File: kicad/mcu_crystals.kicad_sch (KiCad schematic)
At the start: 4 parts, among them X1 32MHz, X2 32kHz768

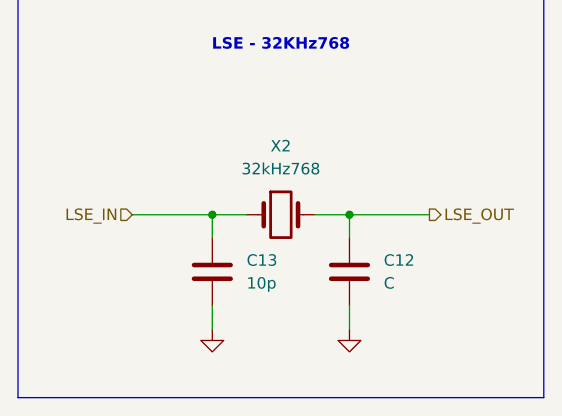
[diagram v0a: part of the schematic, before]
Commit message: fix(schematic:crystals): add the missing value for C12; 10pF
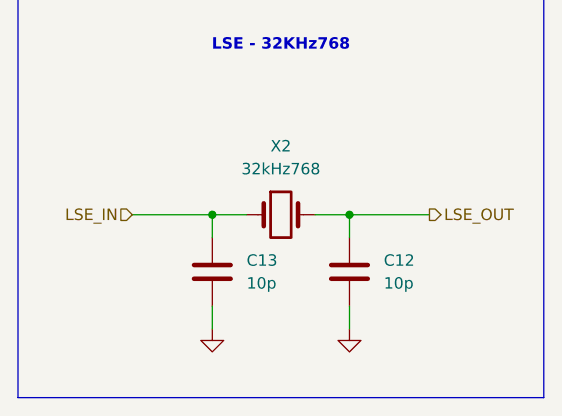
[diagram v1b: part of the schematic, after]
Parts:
- C12: value C -> 10p
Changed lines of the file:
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@@
 			)
 		)
-		(property "Value" "C"
+		(property "Value" "10p"
 			(at 167.64 133.3499 0)
 			(show_name no)
